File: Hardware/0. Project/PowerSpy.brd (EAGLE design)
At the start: 55.5 x 70.5 mm, 83 parts, among them IC1 CP2102N-A01-GQFN28, P1 Mini-Fit 4T, T1 SS8050, T2 SS8050, U1 NCP1117ST33T3G, U2 HLK-PM01, U3 ADS1115IDGST, U4 ESP32-WROOM-32D, X1 4T PJ-321, X2 4T PJ-321, X3 USB Micro B

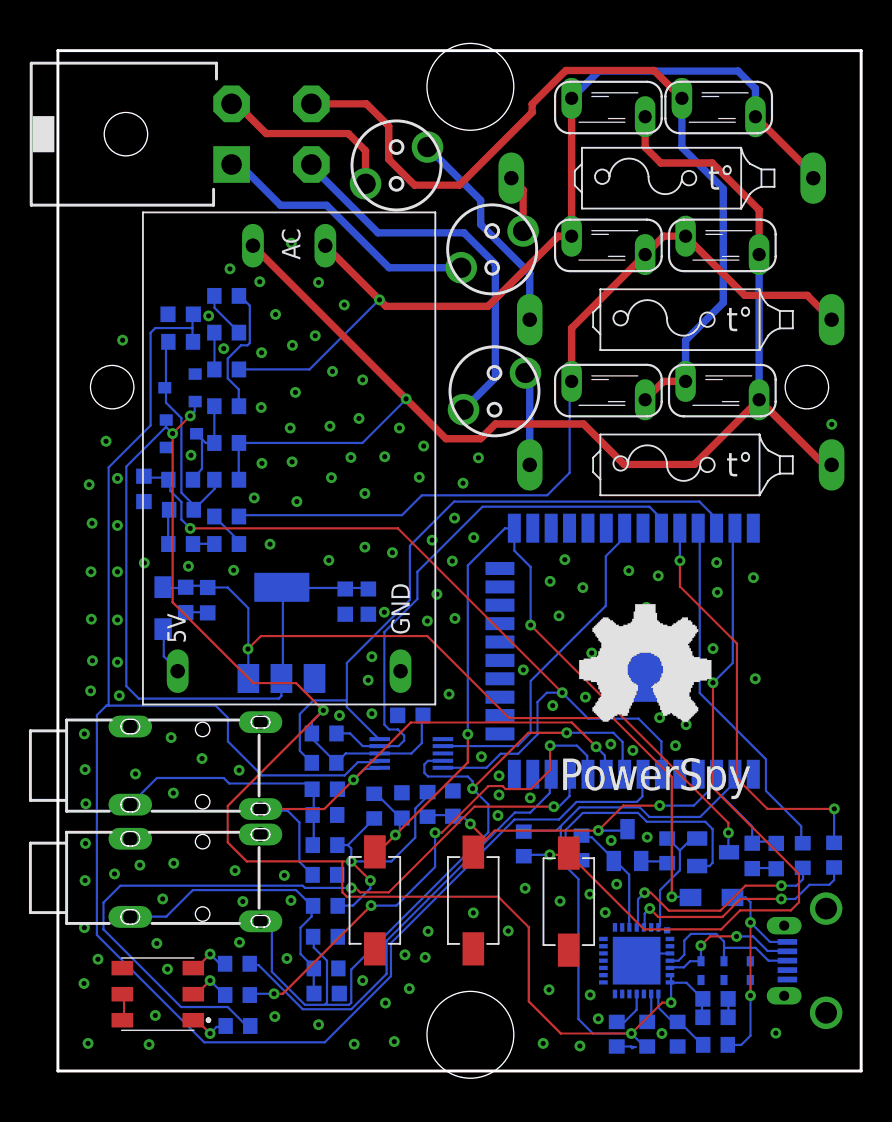
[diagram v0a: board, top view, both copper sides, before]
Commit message: 2.0 PCB created
- Board dimensions resize to match with PB075 Patola case.
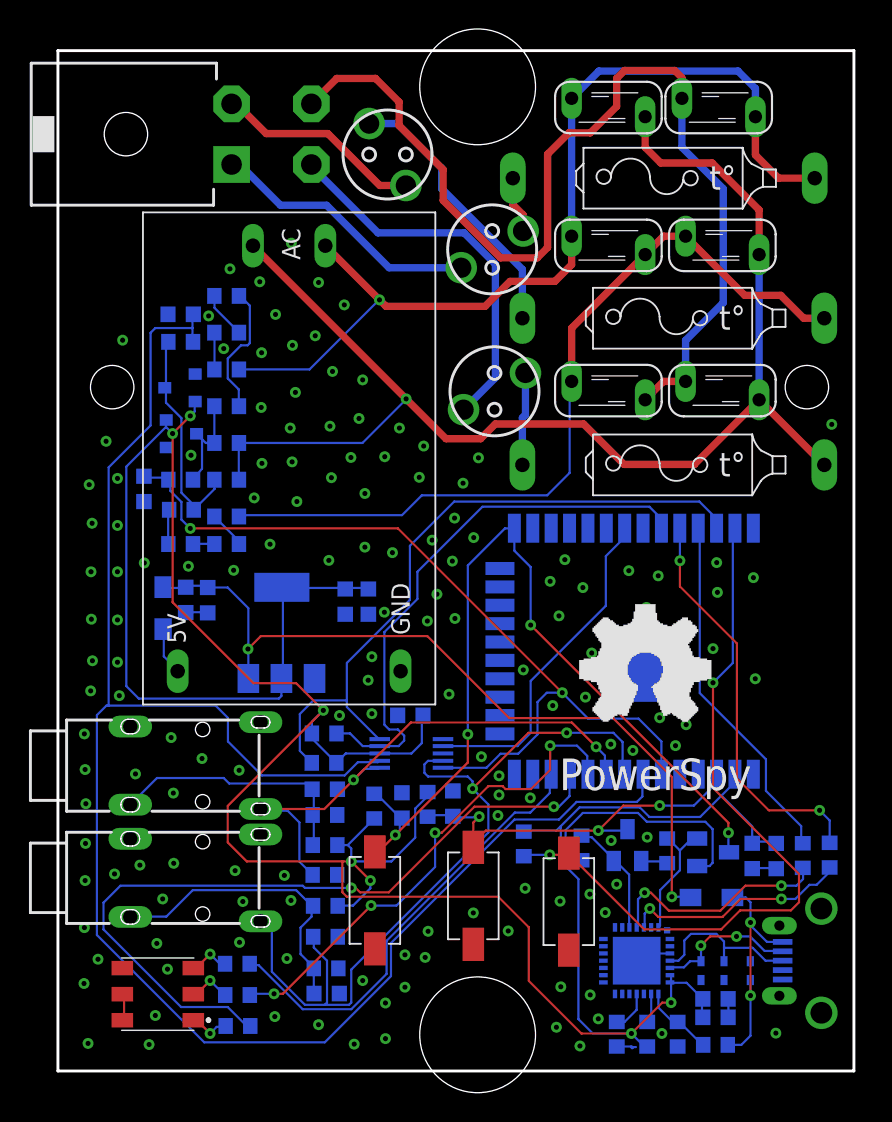
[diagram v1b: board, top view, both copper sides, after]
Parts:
- moved F3 0.98 mm to (22.8, 63.3), turned to 0 degrees
- moved F4 0.52 mm to (42.0, 51.8)
- moved F6 0.51 mm to (42.0, 41.7)
- moved X3 0.33 mm to (54.9, 7.62)
- moved S3 0.32 mm to (28.7, 12.1)
- moved R35 0.30 mm to (53.3, 14.9)
- moved F2 0.10 mm to (41.3, 61.5)
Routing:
- net PE: track 58.8 -> 70.7 mm
- net N$9: track 14.9 -> 19.0 mm
- net L1_VOLTAGE: track 63.8 -> 66.5 mm
- net N$24: track 12.9 -> 14.4 mm
- net EN: track 26.3 -> 27.3 mm
- net 3.3V: track 207.0 -> 206.2 mm
- net USB_TX: track 28.9 -> 28.1 mm
- net N$8: track 16.4 -> 15.7 mm
- net L2_VOLTAGE: track 57.1 -> 56.6 mm
- net NEUTRAL: track 91.1 -> 90.6 mm
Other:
- board size 55.5 x 70.5 mm -> 55 x 70.5 mm

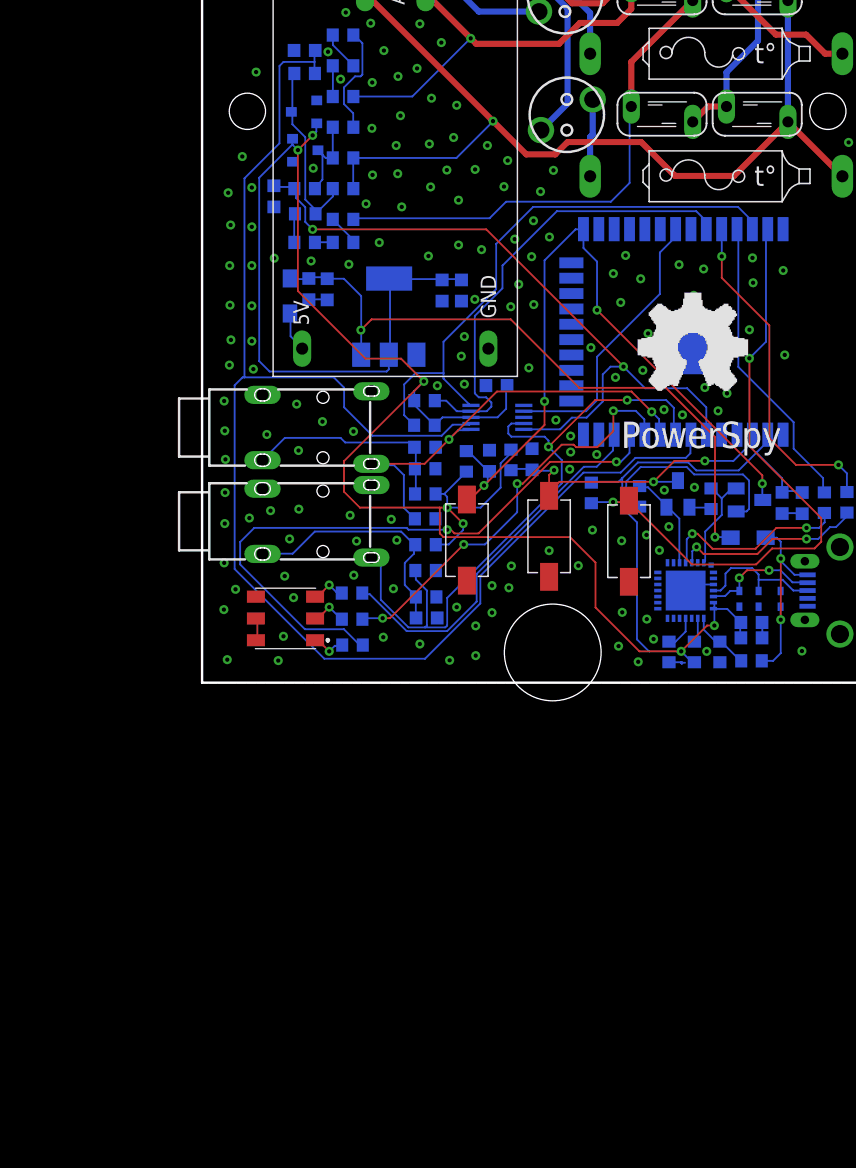
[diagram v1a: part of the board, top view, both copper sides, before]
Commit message: VCC/2 set point added to voltage phase measure channel (WIP)
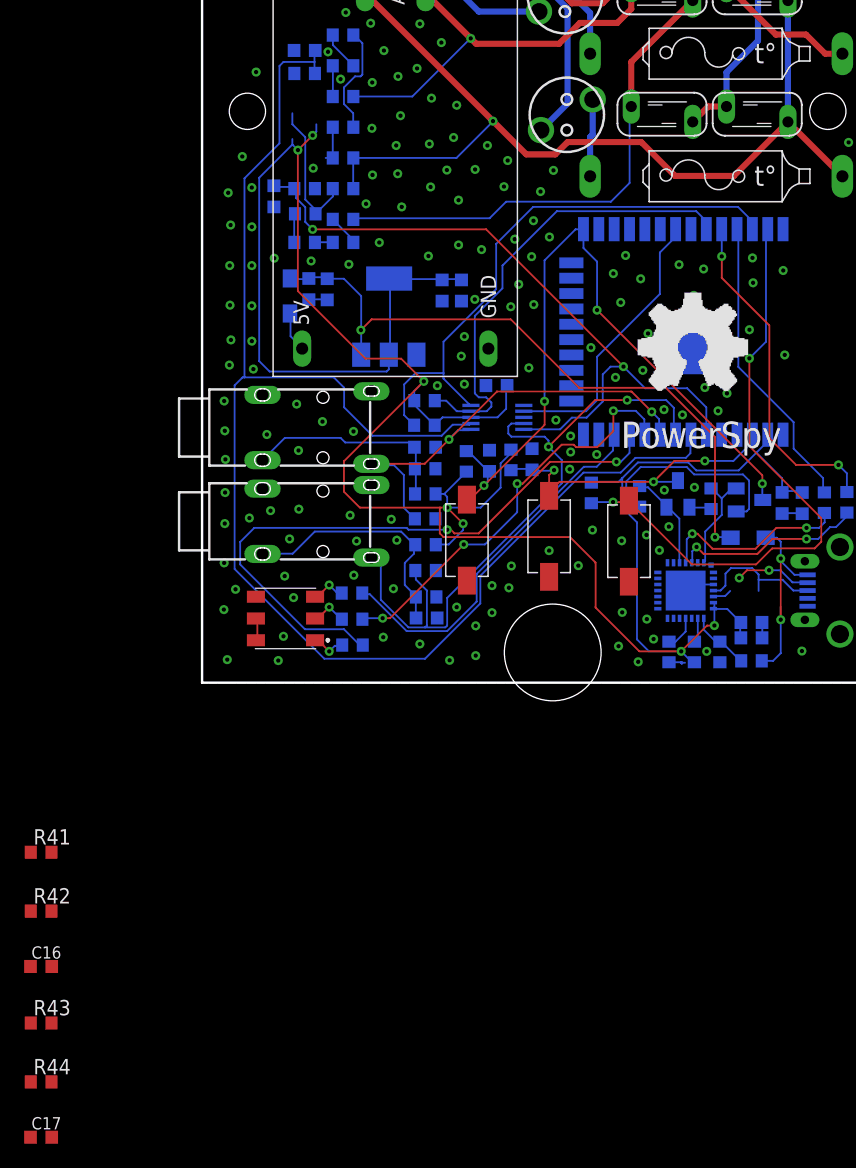
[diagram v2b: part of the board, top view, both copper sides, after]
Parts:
- removed D2, D3: BAV99, BAV99:SOT23-3
- removed D5, D6, D7: ESD5V0D5B, ESD5V0D5B:SOD523
- added C16, C17: 10uF/10V (20%), rcl:C0603K
- added R41, R42, R43, R44: 100k (1%), rcl:R0603
- C5, C6, C9: value 22uF/10V (20%) -> 10uF/10V (20%)
- R20, R28: value 1k (1%) -> 3k3 (1%)
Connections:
- net 3.3V: now also R41.1, R43.1; no longer D2.2, D3.2
- net GND: now also C16.2, C17.2, R42.2, R44.2; no longer D2.1, D3.1, D5.A, D6.A, D7.A
- net N$16: now also C17.1, R43.2, R44.1; no longer D3.3
- net N$20: now also C16.1, R41.2, R42.1; no longer D2.3
- net USB_D+: no longer D5.C
- net USB_D-: no longer D6.C
- net VUSB: no longer D7.C
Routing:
- net N$20: track 7.58 -> 3.13 mm
- net N$16: track 15.2 -> 11.8 mm
- net USB_D-: track 10.3 -> 8.53 mm

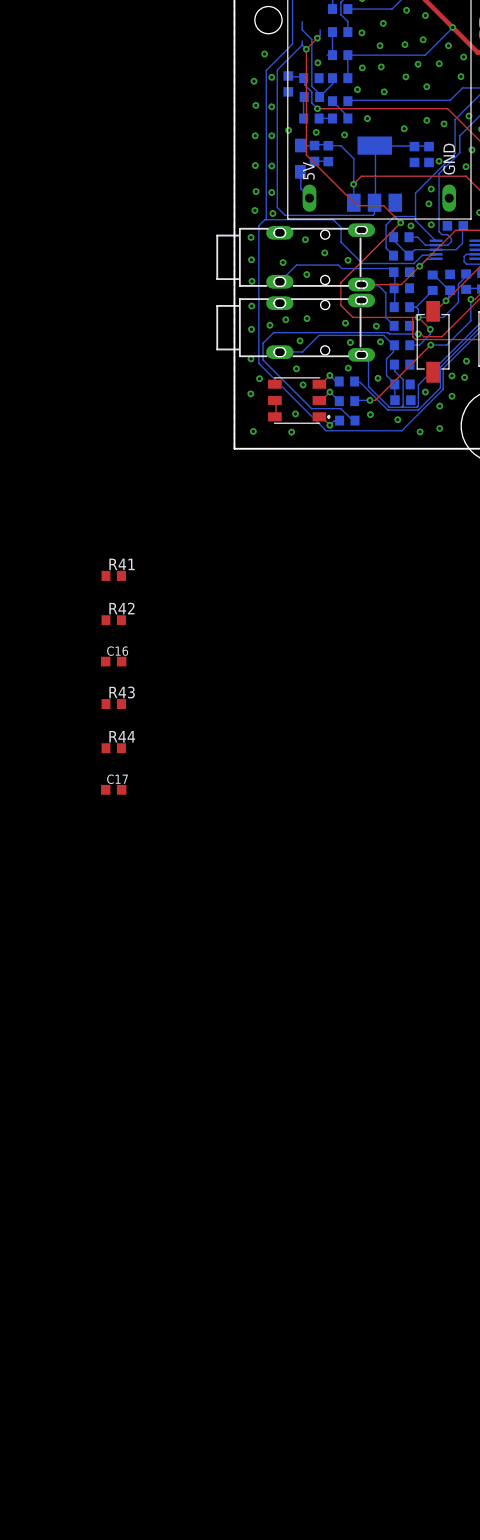
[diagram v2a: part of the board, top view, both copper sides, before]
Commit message: New analog front-end design for voltage measurement
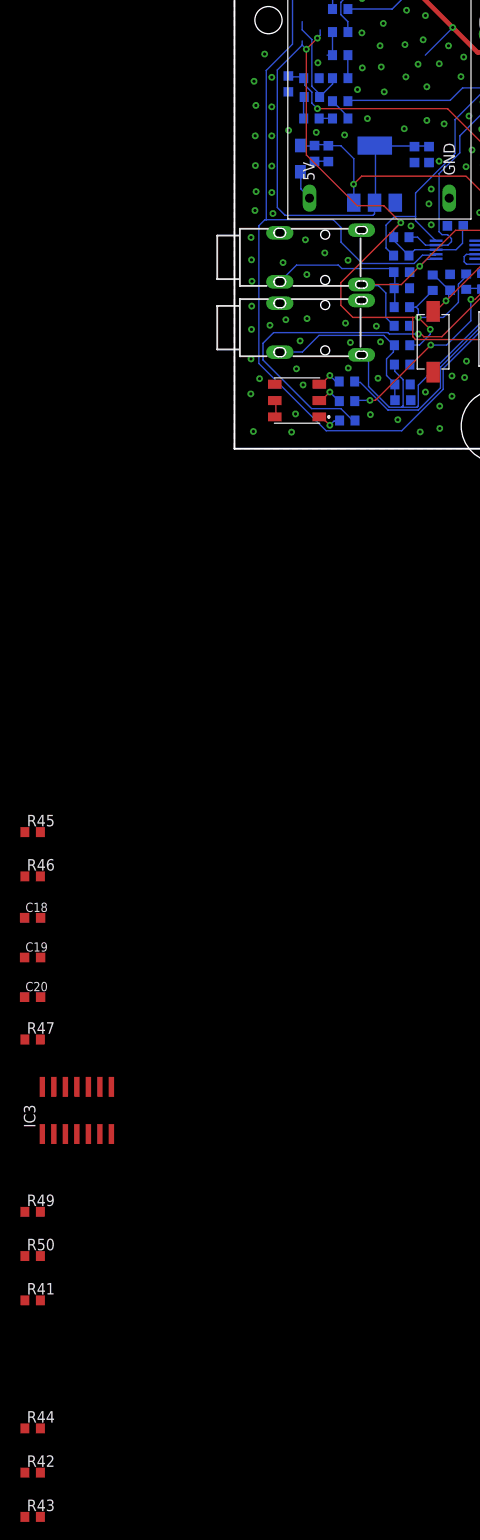
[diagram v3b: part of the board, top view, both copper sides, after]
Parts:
- removed C16, C17: 10uF/10V (20%), rcl:C0603K
- added C18, C20: 10uF/10V (20%), rcl:C0603K
- added C19: 100nF/50V (10%), rcl:C0603K
- added IC3: LM324D, linear:SO14
- added R45, R46, R49, R50: 100k (1%), rcl:R0603
- added R47: 220R (5%), rcl:R0603
- R41, R44: value 100k (1%) -> 220R (5%)
- moved R42 94.4 mm to (-22.3, -112.9)
- moved R43 90.1 mm to (-22.3, -117.8)
- moved R41 80.4 mm to (-22.3, -93.9)
- moved R44 75.5 mm to (-22.3, -108.0)
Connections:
- new net +4.1V: C20.1, IC3.4
- new net N$13: IC3.1, IC3.2, R47.2
- new net N$14: C18.1, C19.1, IC3.3, R45.2, R46.1
- new net N$15: IC3.7, R19.2, R49.1
- new net N$30: IC3.6, R49.2, R50.1
- new net N$31: R18.2, R20.1, R41.2
- new net N$32: IC3.5, R41.1
- new net N$33: IC3.9, R42.2, R43.1
- new net N$34: IC3.10, R44.1
- net 3.3V: now also R45.1; no longer R41.1, R43.1
- net GND: now also C18.2, C19.2, C20.2, IC3.11, R46.2; no longer C16.2, C17.2, R42.2, R44.2
- net N$16: now also R44.2; no longer C17.1, R27.2, R43.2, R44.1
- net N$20: now also IC3.8, R27.2; no longer C16.1, R18.2, R19.2, R20.1, R41.2
- net NEUTRAL: no longer R20.2, R28.2
- net PE: now also R20.2, R28.2, R43.2, R47.1, R50.2
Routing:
- net NEUTRAL: track 90.6 -> 79.5 mm
- net N$31: track 0.00 -> 3.13 mm
- net N$20: track 3.13 -> 0.00 mm
- net PE: track 70.7 -> 73.1 mm

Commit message: Calcs and values updated for the new AFE approach
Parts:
- R20, R28: value 3k3 (1%) -> 1k6 (1%)
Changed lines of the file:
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@@
 <attribute name="VALUE" x="12.293" y="44.029" size="1.27" layer="28" rot="MR0" display="off"/>
 </element>
-<element name="R20" library="rcl" library_urn="urn:adsk.eagle:library:334" package="R0603" package3d_urn="urn:adsk.eagle:package:23555/3" value="3k3 (1%)" x="11.658" y="43.394" smashed="yes" rot="MR180">
+<element name="R20" library="rcl" library_urn="urn:adsk.eagle:library:334" package="R0603" package3d_urn="urn:adsk.eagle:package:23555/3" value="1k6 (1%)" x="11.658" y="43.394" smashed="yes" rot="MR180">
 <attribute name="NAME" x="11.023" y="42.759" size="1.27" layer="26" rot="MR180" display="off"/>
 <attribute name="SPICEPREFIX" value="R" x="101.828" y="141.184" size="1.778" layer="28" rot="MR180" display="off"/>
@@
 <attribute name="VALUE" x="12.293" y="36.409" size="1.27" layer="28" rot="MR0" display="off"/>
 </element>
-<element name="R28" library="rcl" library_urn="urn:adsk.eagle:library:334" package="R0603" package3d_urn="urn:adsk.eagle:package:23555/3" value="3k3 (1%)" x="11.658" y="40.854" smashed="yes" rot="MR180">
+<element name="R28" library="rcl" library_urn="urn:adsk.eagle:library:334" package="R0603" package3d_urn="urn:adsk.eagle:package:23555/3" value="1k6 (1%)" x="11.658" y="40.854" smashed="yes" rot="MR180">
 <attribute name="NAME" x="11.023" y="40.219" size="1.27" layer="26" rot="MR180" display="off"/>
 <attribute name="SPICEPREFIX" value="R" x="30.708" y="143.724" size="1.778" layer="28" rot="MR180" display="off"/>
